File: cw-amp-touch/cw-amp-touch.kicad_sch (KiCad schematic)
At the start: 11 parts, among them J1 Conn_02x05_Odd_Even

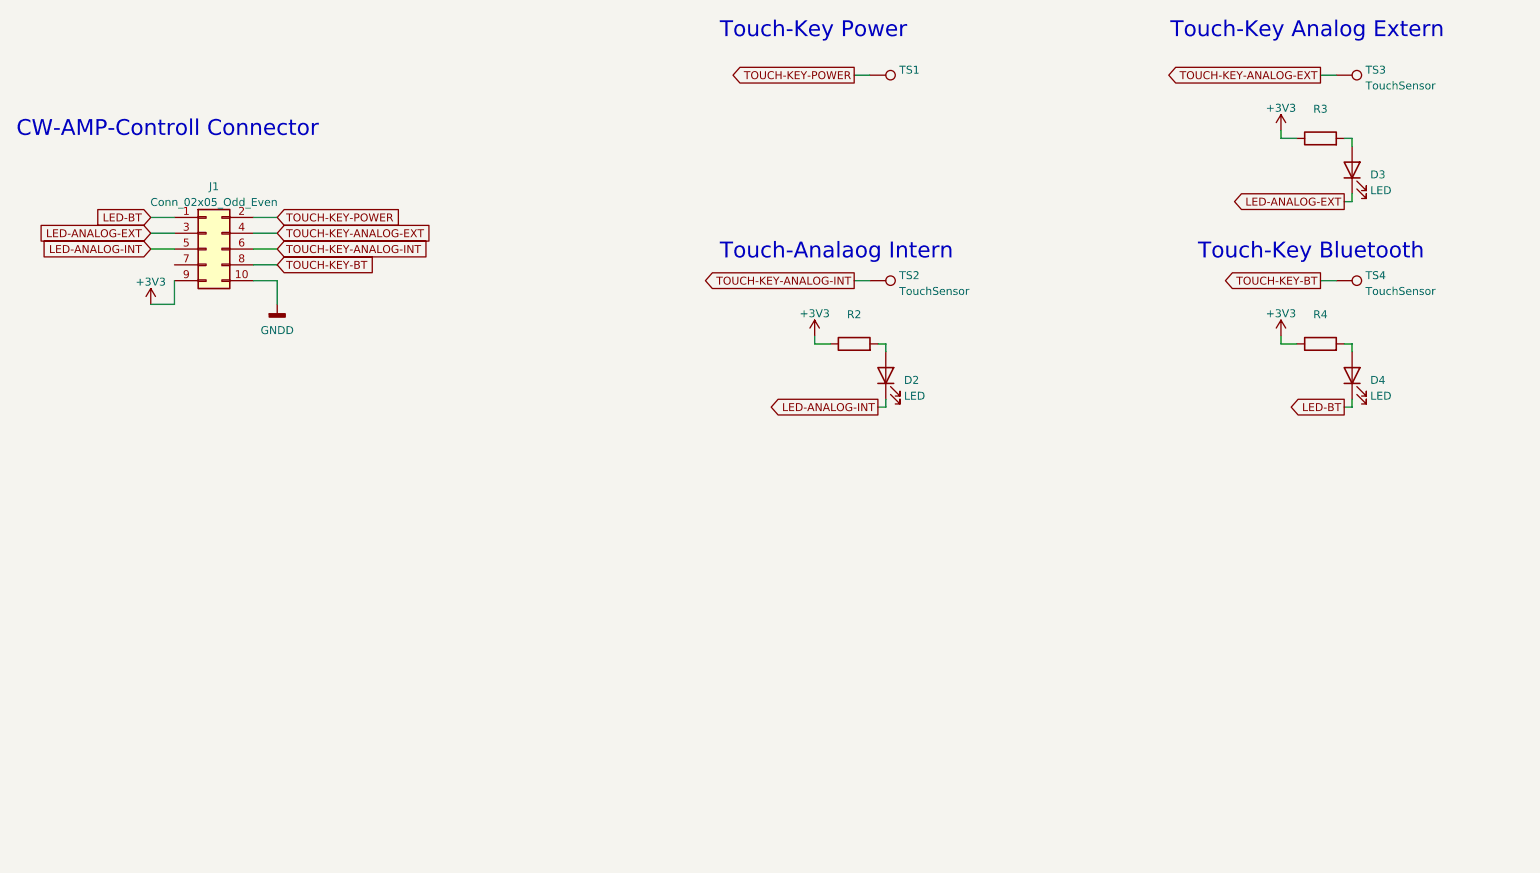
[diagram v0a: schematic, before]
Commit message: office amp touch: replaced IDC through hole with SMD pinheader
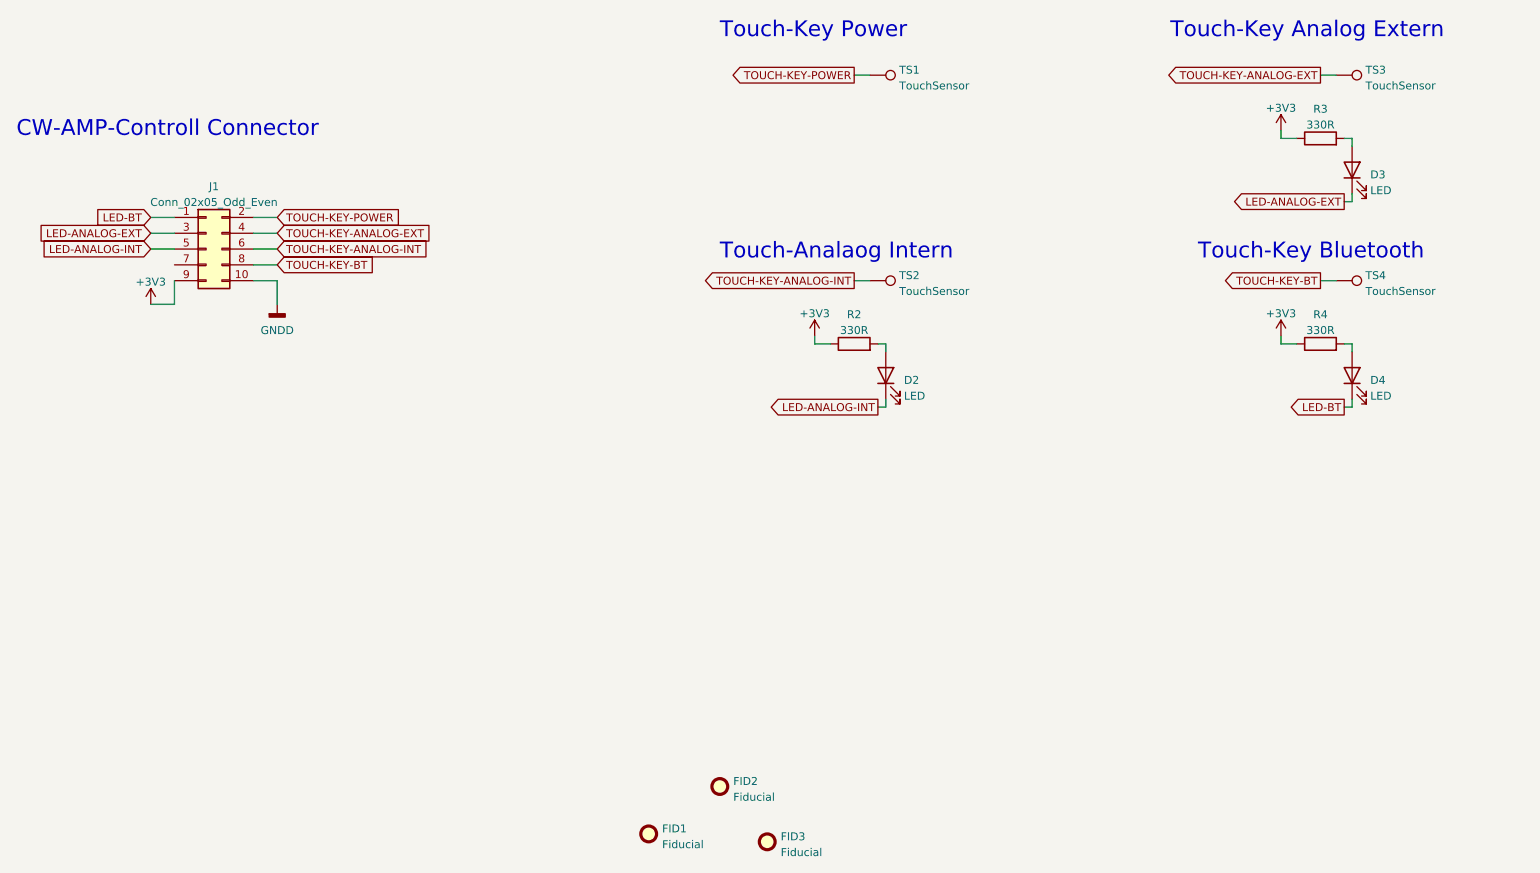
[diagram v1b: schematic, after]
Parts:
- added FID1, FID2, FID3: Fiducial, Fiducial:Fiducial_1.5mm_Mask3mm, symbol Mechanical:Fiducial
- D2, D3, D4: footprint (none) -> office-amp:LED-5mm-ThroughPCB
- J1: footprint Connector_IDC:IDC-Header_2x05_P2.54mm_Vertical -> Connector_PinHeader_2.54mm:PinHeader_2x05_P2.54mm_Vertical_SMD
- R2, R3, R4: value (none) -> 330R; footprint (none) -> Resistor_SMD:R_0805_2012Metric_Pad1.20x1.40mm_HandSolder
- TS1: value (none) -> TouchSensor; footprint (none) -> office-amp:TouchSensor
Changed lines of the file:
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@@
     (in_bom yes) (on_board yes) (fields_autoplaced)
     (property "Reference" "R4" (id 0) (at 238.76 105.7742 90))
-    (property "Value" "" (id 1) (at 238.76 108.3111 90))
-    (property "Footprint" "" (id 2) (at 238.76 112.268 90)
+    (property "Value" "330R" (id 1) (at 238.76 108.3111 90))
+    (property "Footprint" "Resistor_SMD:R_0805_2012Metric_Pad1.20x1.40mm_HandSolder" (id 2) (at 238.76 112.268 90)
       (effects (font (size 1.27 1.27)) hide)
     )
@@
       (effects (font (size 1.27 1.27)) (justify right))
     )
-    (property "Footprint" "" (id 2) (at 243.84 82.55 0)
+    (property "Footprint" "office-amp:LED-5mm-ThroughPCB" (id 2) (at 243.84 82.55 0)
       (effects (font (size 1.27 1.27)) hide)
     )
@@
       (effects (font (size 1.27 1.27)) (justify right))
     )
-    (property "Footprint" "" (id 2) (at 168.91 115.57 0)
+    (property "Footprint" "office-amp:LED-5mm-ThroughPCB" (id 2) (at 168.91 115.57 0)
       (effects (font (size 1.27 1.27)) hide)
     )
@@
       (effects (font (size 1.27 1.27)) (justify right))
     )
-    (property "Footprint" "" (id 2) (at 243.84 115.57 0)
+    (property "Footprint" "office-amp:LED-5mm-ThroughPCB" (id 2) (at 243.84 115.57 0)
       (effects (font (size 1.27 1.27)) hide)
     )
@@
     (pin "1")
     (pin "2")
+  )
+  (symbol (lib_id "Mechanical:Fiducial") (at 142.24 181.61 0) (unit 1)
+    (in_bom yes) (on_board yes) (fields_autoplaced)
+    (property "Reference" "FID2" (id 0) (at 144.399 180.7753 0)
+      (effects (font (size 1.27 1.27)) (justify left))
+    )
+    (property "Value" "Fiducial" (id 1) (at 144.399 183.3122 0)
+      (effects (font (size 1.27 1.27)) (justify left))
+    )
+    (property "Footprint" "Fiducial:Fiducial_1.5mm_Mask3mm" (id 2) (at 142.24 181.61 0)
+      (effects (font (size 1.27 1.27)) hide)
+    )
+    (property "Datasheet" "~" (id 3) (at 142.24 181.61 0)
+      (effects (font (size 1.27 1.27)) hide)
+    )
   )
   (symbol (lib_id "Connector_Generic:Conn_02x05_Odd_Even") (at 59.69 95.25 0) (unit 1)
@@
     (property "Reference" "J1" (id 0) (at 60.96 85.2002 0))
     (property "Value" "Conn_02x05_Odd_Even" (id 1) (at 60.96 87.7371 0))
-    (property "Footprint" "Connector_IDC:IDC-Header_2x05_P2.54mm_Vertical" (id 2) (at 59.69 95.25 0)
+    (property "Footprint" "Connector_PinHeader_2.54mm:PinHeader_2x05_P2.54mm_Vertical_SMD" (id 2) (at 59.69 95.25 0)
       (effects (font (size 1.27 1.27)) hide)
     )
@@
     (in_bom yes) (on_board yes) (fields_autoplaced)
     (property "Reference" "R3" (id 0) (at 238.76 72.7542 90))
-    (property "Value" "" (id 1) (at 238.76 75.2911 90))
-    (property "Footprint" "" (id 2) (at 238.76 79.248 90)
+    (property "Value" "330R" (id 1) (at 238.76 75.2911 90))
+    (property "Footprint" "Resistor_SMD:R_0805_2012Metric_Pad1.20x1.40mm_HandSolder" (id 2) (at 238.76 79.248 90)
       (effects (font (size 1.27 1.27)) hide)
     )
@@
     (in_bom yes) (on_board yes) (fields_autoplaced)
     (property "Reference" "R2" (id 0) (at 163.83 105.7742 90))
-    (property "Value" "" (id 1) (at 163.83 108.3111 90))
-    (property "Footprint" "" (id 2) (at 163.83 112.268 90)
+    (property "Value" "330R" (id 1) (at 163.83 108.3111 90))
+    (property "Footprint" "Resistor_SMD:R_0805_2012Metric_Pad1.20x1.40mm_HandSolder" (id 2) (at 163.83 112.268 90)
       (effects (font (size 1.27 1.27)) hide)
     )
@@
       (effects (font (size 1.27 1.27)) (justify left))
     )
-    (property "Value" "" (id 1) (at 171.069 69.0122 90)
-      (effects (font (size 1.27 1.27)) (justify left))
-    )
-    (property "Footprint" "" (id 2) (at 166.37 72.39 0)
+    (property "Value" "TouchSensor" (id 1) (at 171.069 69.0122 90)
+      (effects (font (size 1.27 1.27)) (justify left))
+    )
+    (property "Footprint" "office-amp:TouchSensor" (id 2) (at 166.37 72.39 0)
       (effects (font (size 1.27 1.27)) hide)
     )
@@
     )
     (pin "1")
+  )
+  (symbol (lib_id "Mechanical:Fiducial") (at 130.81 189.23 0) (unit 1)
+    (in_bom yes) (on_board yes) (fields_autoplaced)
+    (property "Reference" "FID1" (id 0) (at 132.969 188.3953 0)
+      (effects (font (size 1.27 1.27)) (justify left))
+    )
+    (property "Value" "Fiducial" (id 1) (at 132.969 190.9322 0)
+      (effects (font (size 1.27 1.27)) (justify left))
+    )
+    (property "Footprint" "Fiducial:Fiducial_1.5mm_Mask3mm" (id 2) (at 130.81 189.23 0)
+      (effects (font (size 1.27 1.27)) hide)
+    )
+    (property "Datasheet" "~" (id 3) (at 130.81 189.23 0)
+      (effects (font (size 1.27 1.27)) hide)
+    )
+  )
+  (symbol (lib_id "Mechanical:Fiducial") (at 149.86 190.5 0) (unit 1)
+    (in_bom yes) (on_board yes) (fields_autoplaced)
+    (property "Reference" "FID3" (id 0) (at 152.019 189.6653 0)
+      (effects (font (size 1.27 1.27)) (justify left))
+    )
+    (property "Value" "Fiducial" (id 1) (at 152.019 192.2022 0)
+      (effects (font (size 1.27 1.27)) (justify left))
+    )
+    (property "Footprint" "Fiducial:Fiducial_1.5mm_Mask3mm" (id 2) (at 149.86 190.5 0)
+      (effects (font (size 1.27 1.27)) hide)
+    )
+    (property "Datasheet" "~" (id 3) (at 149.86 190.5 0)
+      (effects (font (size 1.27 1.27)) hide)
+    )
   )
   (symbol (lib_id "power:GNDD") (at 71.12 104.14 0) (unit 1)
@@
       (reference "D4") (unit 1) (value "LED") (footprint "office-amp:LED-5mm-ThroughPCB")
     )
+    (path "/ce071a60-a5bb-4fc8-865b-380a85718362"
+      (reference "FID1") (unit 1) (value "Fiducial") (footprint "Fiducial:Fiducial_1.5mm_Mask3mm")
+    )
+    (path "/79219506-353a-4414-96cf-c27c8263c22f"
+      (reference "FID2") (unit 1) (value "Fiducial") (footprint "Fiducial:Fiducial_1.5mm_Mask3mm")
+    )
+    (path "/da7b836a-3d1f-4e42-8f0b-2d01ac10dcf1"
+      (reference "FID3") (unit 1) (value "Fiducial") (footprint "Fiducial:Fiducial_1.5mm_Mask3mm")
+    )
     (path "/9aa4051b-5d8e-420b-bd92-028862775303"
-      (reference "J1") (unit 1) (value "Conn_02x05_Odd_Even") (footprint "Connector_IDC:IDC-Header_2x05_P2.54mm_Vertical")
+      (reference "J1") (unit 1) (value "Conn_02x05_Odd_Even") (footprint "Connector_PinHeader_2.54mm:PinHeader_2x05_P2.54mm_Vertical_SMD")
     )
     (path "/b547536e-820e-4276-a2e8-8ade1afd55a1"
